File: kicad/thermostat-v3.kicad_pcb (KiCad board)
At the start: 2 copper layers, 140 x 64 mm, 91 parts, among them J1 HVAC R C W Y G, J2 USB-C, J3 Stemma QT, J4 2.9in EPD FPC, Q1 SI1308EDL, Q2 BT136S-600D, Q3 BT136S-600D, Q4 BT136S-600D, SW1 RESET, SW2 BOOT, SW3 UP, SW4 DOWN, SW5 MODE, U1 LMR16006XDDCR, U2 USBLC6-2SC6, U3 ESP32-C6-WROOM-1-N8, U4 STWD100NYWY3F, U5 SHT40-AD1B, U6 MOC3063S, U7 MOC3063S, U8 MOC3063S

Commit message: Display fit check: GDEY029T94 placement, fold geometry, overlay image; move panel outline on Cmts.User
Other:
- board text added: "2.9in EPD outline, 5mm above PCB (FPC exits right edge, folded under, contacts down) - see fab/display-fit.png"
- board text removed: "2.9in EPD panel outline (FPC exits right edge, folded under, contacts down)"
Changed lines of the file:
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@@
 	)
 	(gr_line
-		(start 209 125)
-		(end 209 161.7)
-		(stroke
-			(width 0.15)
-			(type default)
-		)
-		(layer "Cmts.User")
-	)
-	(gr_line
-		(start 209 161.7)
-		(end 130 161.7)
-		(stroke
-			(width 0.15)
-			(type default)
-		)
-		(layer "Cmts.User")
-	)
-	(gr_line
-		(start 130 125)
-		(end 209 125)
-		(stroke
-			(width 0.15)
-			(type default)
-		)
-		(layer "Cmts.User")
-	)
-	(gr_line
-		(start 130 161.7)
-		(end 130 125)
+		(start 208.46 126.24)
+		(end 208.46 162.94)
+		(stroke
+			(width 0.15)
+			(type default)
+		)
+		(layer "Cmts.User")
+	)
+	(gr_line
+		(start 208.46 162.94)
+		(end 129.46 162.94)
+		(stroke
+			(width 0.15)
+			(type default)
+		)
+		(layer "Cmts.User")
+	)
+	(gr_line
+		(start 129.46 126.24)
+		(end 208.46 126.24)
+		(stroke
+			(width 0.15)
+			(type default)
+		)
+		(layer "Cmts.User")
+	)
+	(gr_line
+		(start 129.46 162.94)
+		(end 129.46 126.24)
 		(stroke
 			(width 0.15)
@@
 		)
 	)
-	(gr_text "2.9in EPD panel outline (FPC exits right edge, folded under, contacts down)"
-		(at 169.5 126.5 0)
-		(layer "Cmts.User")
-		(effects
+	(gr_text "2.9in EPD outline, 5mm above PCB (FPC exits right edge, folded under, contacts down) - see fab/display-fit.png"
+		(at 169 127.7 0)
+		(layer "Cmts.User")
+		(effects

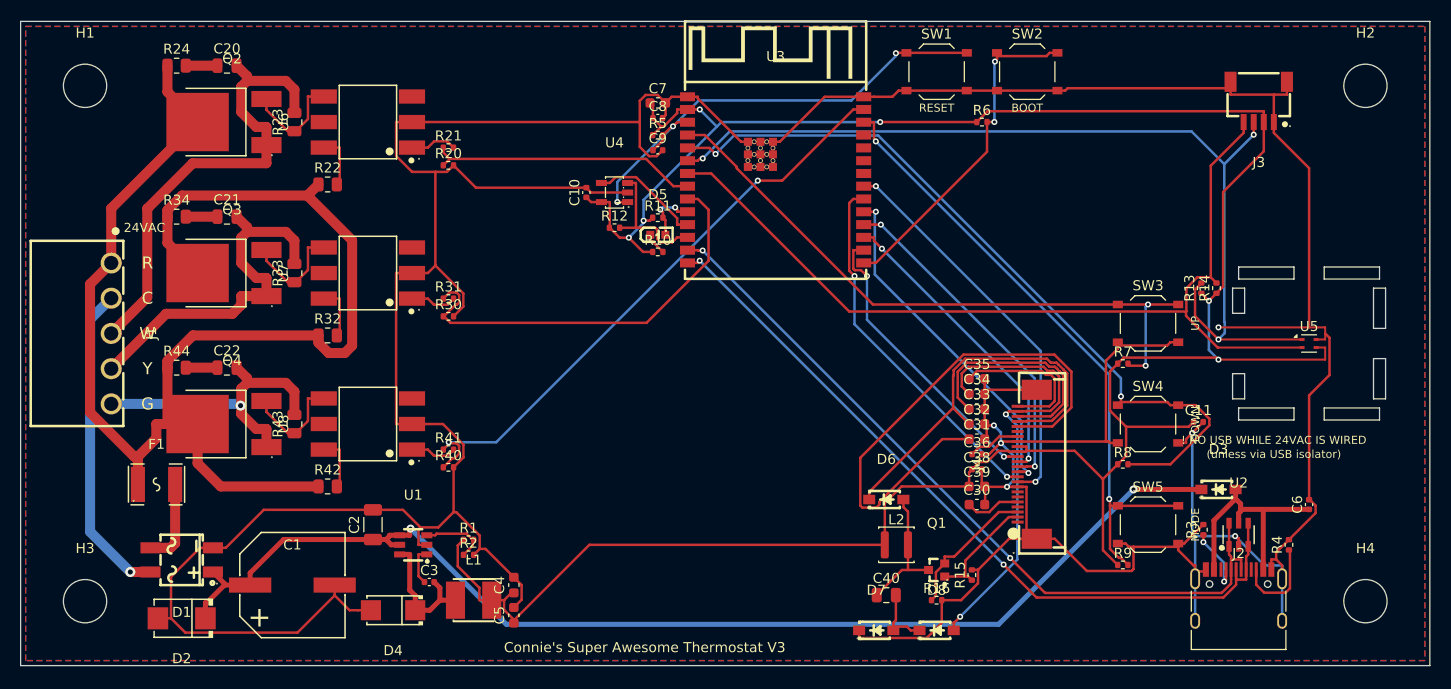
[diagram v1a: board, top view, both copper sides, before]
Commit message: V3 rev4: fix CPL/gerber origin, switch BOM grouping, basic-part swaps, silkscreen cleanup, cat logo
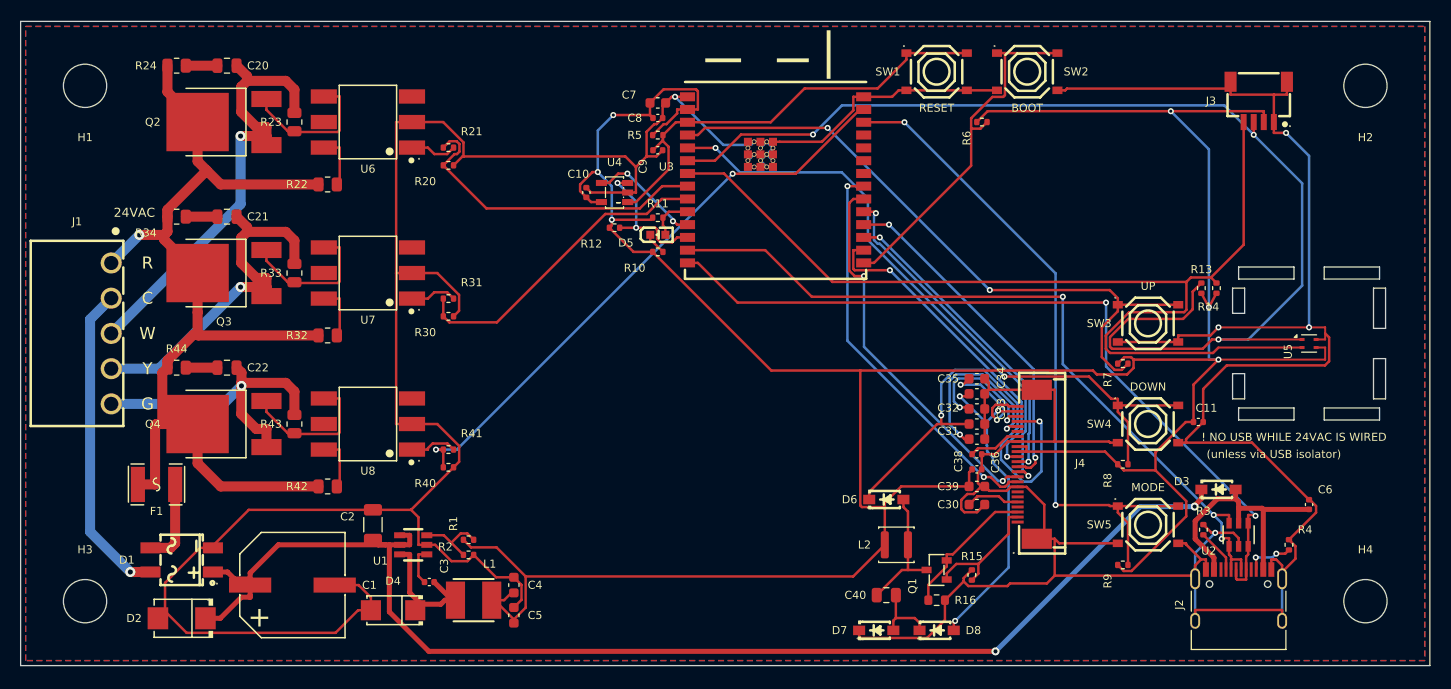
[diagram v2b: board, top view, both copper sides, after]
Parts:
- added LOGO1: LOGO, LOGO_CAT, B.Cu at (188.0, 145.0)
- C2: value 2.2uF 100V -> 2.2uF 50V
- Q1: value SI1308EDL -> AO3400A; footprint tstat:SOT-323_SI1308 -> tstat:SOT-23_AO3400A
- R16: footprint Resistor_SMD:R_0402_1005Metric -> Resistor_SMD:R_0603_1608Metric
- SW1, SW2, SW3, SW4, SW5: footprint Button_Switch_SMD:SW_Push_1P1T_XKB_TS-1187A -> tstat:SW_TS1187A
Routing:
- net +3V3: track 257.8 -> 314.0 mm
- net HVAC_R: track 141.8 -> 100.9 mm, vias 0 -> 1
- net EPD_VSH1: track 54.2 -> 18.6 mm, vias 0 -> 2
- net I2C_SDA: track 94.1 -> 121.4 mm
- net I2C_SCL: track 91.2 -> 107.3 mm
- net EPD_VGL: track 45.6 -> 32.2 mm, vias 2 -> 3
- net VIN_HV: track 117.5 -> 128.4 mm
- net EPD_VSL: track 23.4 -> 13.2 mm, vias 0 -> 2
- net DRV_Y: track 41.5 -> 31.3 mm
- net BTN_DOWN: track 76.7 -> 68.4 mm
- net EPD_VGH: track 39.7 -> 45.8 mm, vias 0 -> 2
- net DRV_W: track 27.0 -> 31.9 mm
- net BTN_MODE: track 62.4 -> 66.8 mm
- net CC2: track 9.22 -> 4.83 mm, vias 0 -> 2
- net GATE_Y: track 10.4 -> 14.3 mm
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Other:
- board text added: "Connie's Super Awesome Thermostat VERSION 3.0"
- board text removed: "Connie's Super Awesome Thermostat V3"

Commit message: V3 rev5: rear vertical HVAC terminal, low-profile C1, SHT40 island net rule, 3D-printable case (OpenSCAD/STL/3MF)
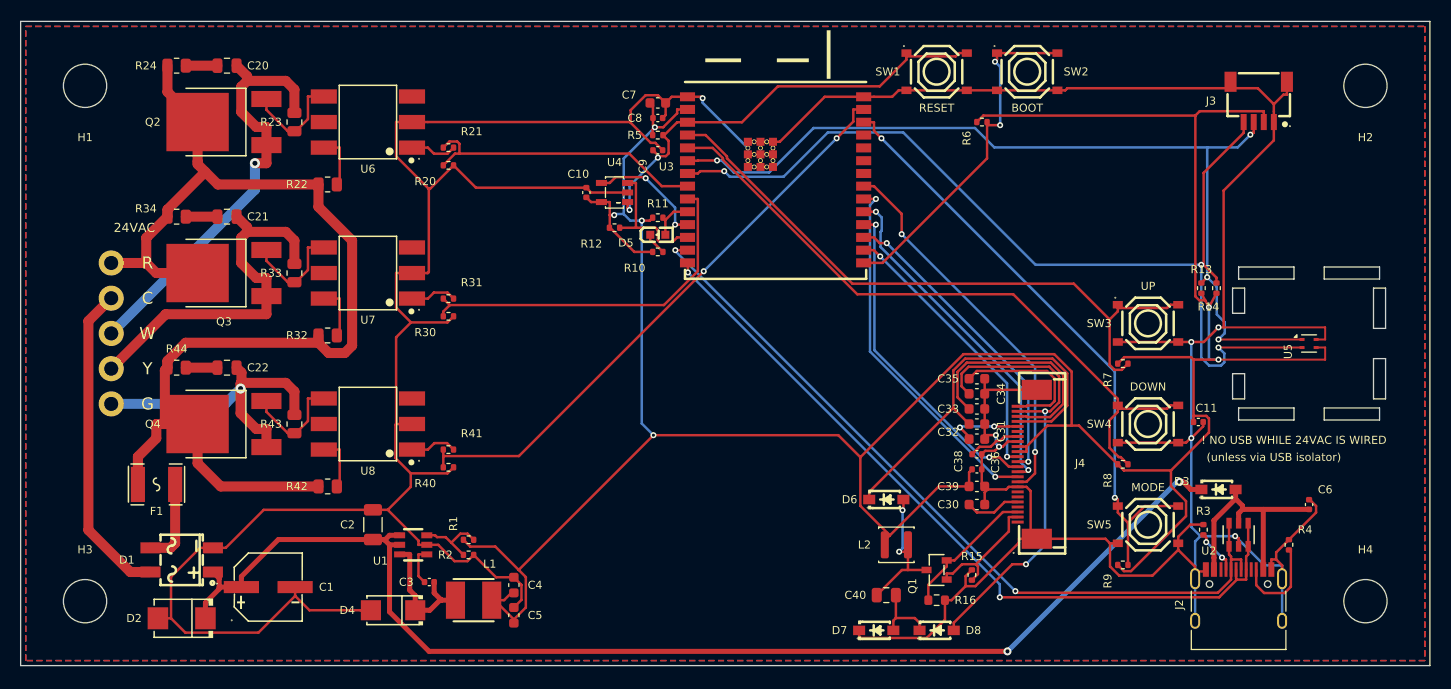
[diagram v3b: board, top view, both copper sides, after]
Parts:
- C1: value 100uF 63V -> 22uF 50V; footprint tstat:CP_10x10_RVT -> tstat:CP_6.3x5.4_RVT
- J1: footprint tstat:HVAC_TERM_15EDGRC -> tstat:HVAC_TERM_15EDGVC; moved to B.Cu
- moved C1 2.41 mm to (124.6, 156.2)
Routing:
- net I2C_SDA: track 121.4 -> 90.2 mm, vias 3 -> 4
- net GND: track 495.3 -> 464.3 mm, vias 5 -> 7
- net +3V3: track 314.0 -> 295.8 mm
- net HVAC_R: track 100.9 -> 116.4 mm, vias 1 -> 0
- net EPD_VGL: track 32.2 -> 46.1 mm, vias 3 -> 2
- net EPD_VSH1: track 18.6 -> 7.32 mm
- net EPD_VSL: track 13.2 -> 23.5 mm, vias 2 -> 0
- net I2C_SCL: track 107.3 -> 99.0 mm, vias 0 -> 3
- net EPD_VGH: track 45.8 -> 39.7 mm, vias 2 -> 0
- net BTN_MODE: track 66.8 -> 61.2 mm
- net DRV_Y: track 31.3 -> 36.5 mm
- net CC2: track 4.83 -> 9.31 mm, vias 2 -> 0
- net VIN_HV: track 128.4 -> 124.0 mm
- net EPD_MOSI: track 32.2 -> 28.1 mm
- net GATE_Y: track 14.3 -> 10.4 mm
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
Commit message: V3 rev6: drywall-anchor case (146x70), multi-colour AMS parts + 3MF, no USB opening, 100V X7R bulk caps
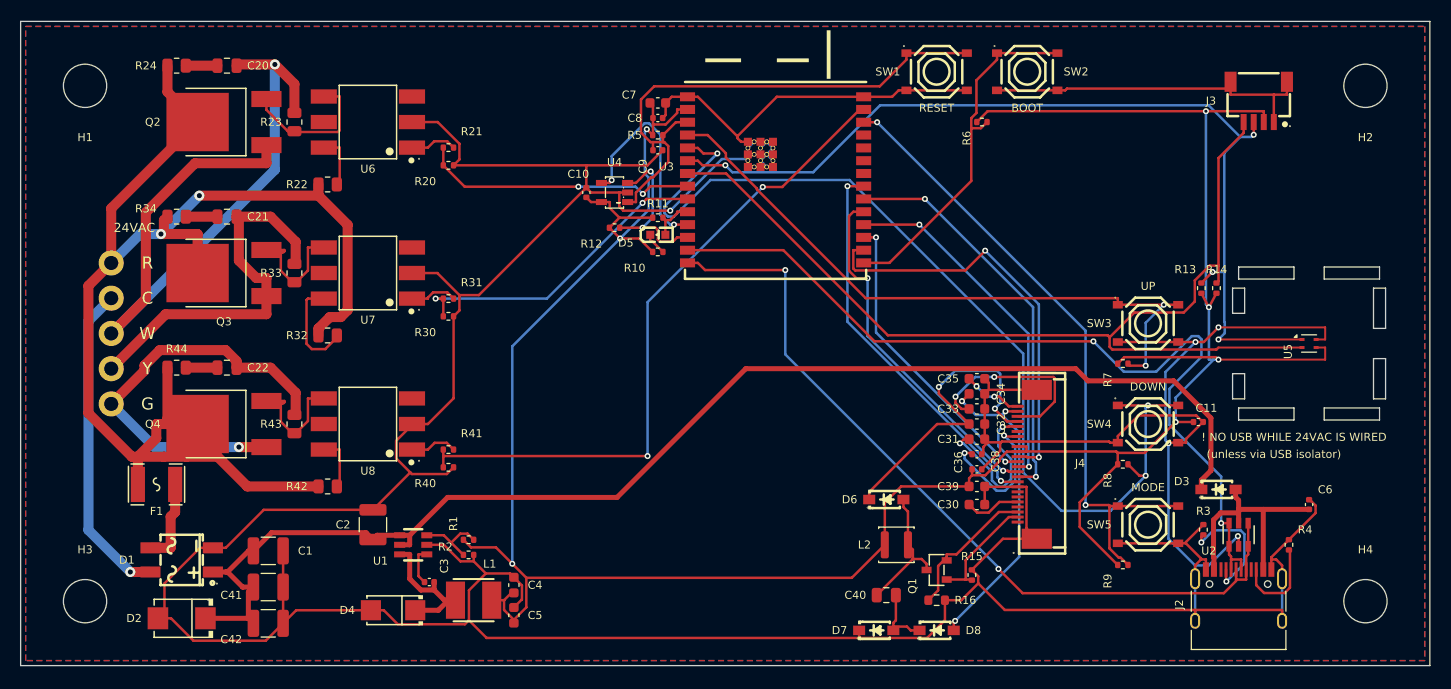
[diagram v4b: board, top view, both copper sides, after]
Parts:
- added C41: 4.7uF 100V X7R, Capacitor_SMD:C_1210_3225Metric, F.Cu at (124.6, 156.2)
- added C42: 4.7uF 100V X7R, Capacitor_SMD:C_1210_3225Metric, F.Cu at (124.6, 159.8)
- C1: value 22uF 50V -> 4.7uF 100V X7R; footprint tstat:CP_6.3x5.4_RVT -> Capacitor_SMD:C_1210_3225Metric
- C2: value 2.2uF 50V -> 4.7uF 100V X7R; footprint Capacitor_SMD:C_1206_3216Metric -> Capacitor_SMD:C_1210_3225Metric
- moved C1 3.60 mm to (124.6, 152.6)
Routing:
- net GND: track 464.3 -> 525.0 mm, vias 7 -> 5
- net BTN_DOWN: track 67.0 -> 98.0 mm, vias 0 -> 3
- net HVAC_W: track 43.3 -> 72.2 mm
- net +3V3: track 295.8 -> 271.4 mm, vias 6 -> 7
- net HVAC_R: track 116.4 -> 133.6 mm, vias 0 -> 2
- net EPD_VGL: track 46.1 -> 32.1 mm, vias 2 -> 3
- net EPD_MOSI: track 28.1 -> 41.7 mm
- net HVAC_G: track 31.2 -> 42.4 mm
- net WD_WDI: track 11.7 -> 21.3 mm
- net EPD_VCOM: track 15.3 -> 5.97 mm, vias 0 -> 2
- net EPD_VDD: track 5.26 -> 14.5 mm, vias 0 -> 2
- net EPD_VSH1: track 7.32 -> 16.2 mm
- net DRV_G: track 58.5 -> 66.7 mm
- net ESP_EN: track 45.4 -> 53.5 mm, vias 2 -> 0
- net USB_DN: track 78.8 -> 86.8 mm
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
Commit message: V3 rev7: rear right-angle HVAC terminal beside centred wire hole, deeper case standoffs
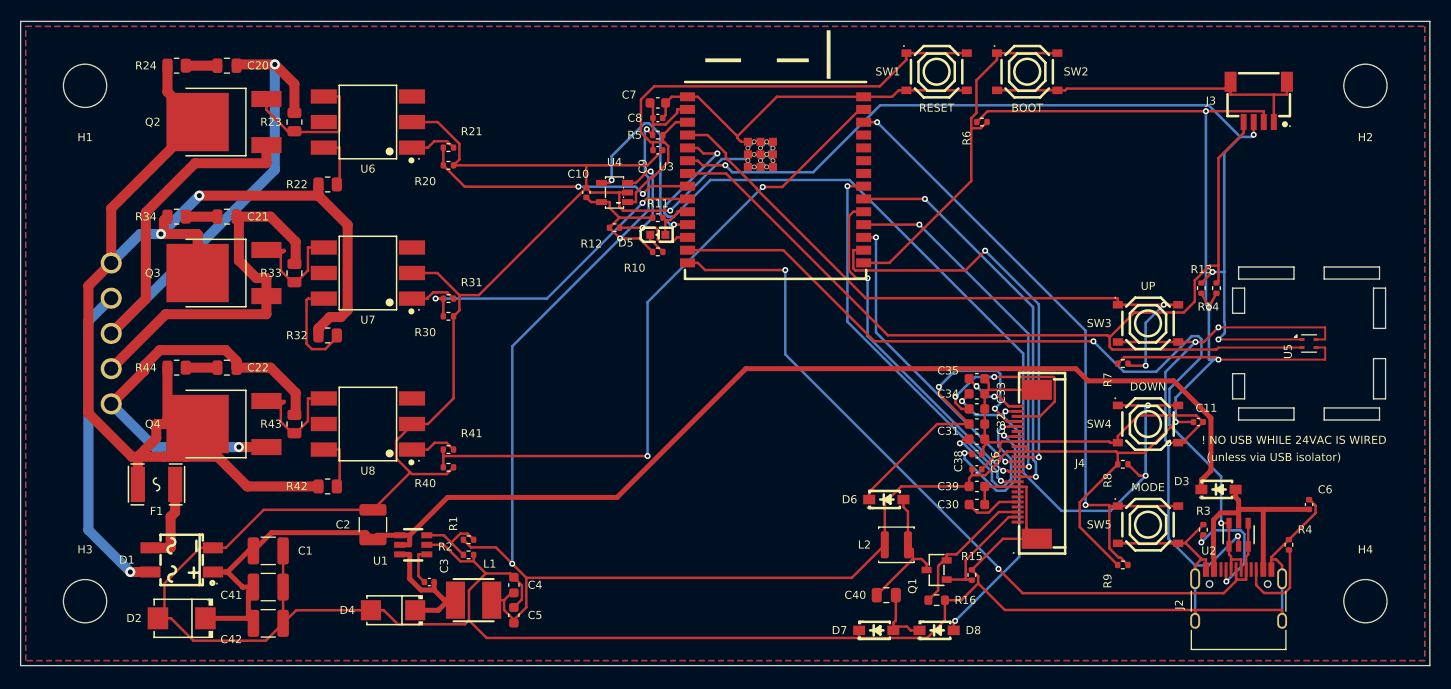
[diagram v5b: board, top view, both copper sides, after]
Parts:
- J1: footprint tstat:HVAC_TERM_15EDGVC -> tstat:HVAC_TERM_15EDGRC
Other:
- board text added: "24VAC HVAC (plug: 15EDGK-3.5-05P)"
- board text removed: "24VAC"

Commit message: Rev 8: review fixes - J1 really at (70,58) rear, D3 SS210 100V, F1 60V PTC, SHDN 100k, C43 47uF/63V rear THT, T435-600B standard-gate triacs, antenna keepout, USB-C flush, 1mm HV pour clearance, test pads; case RESET pinhole; generator scripts + review response
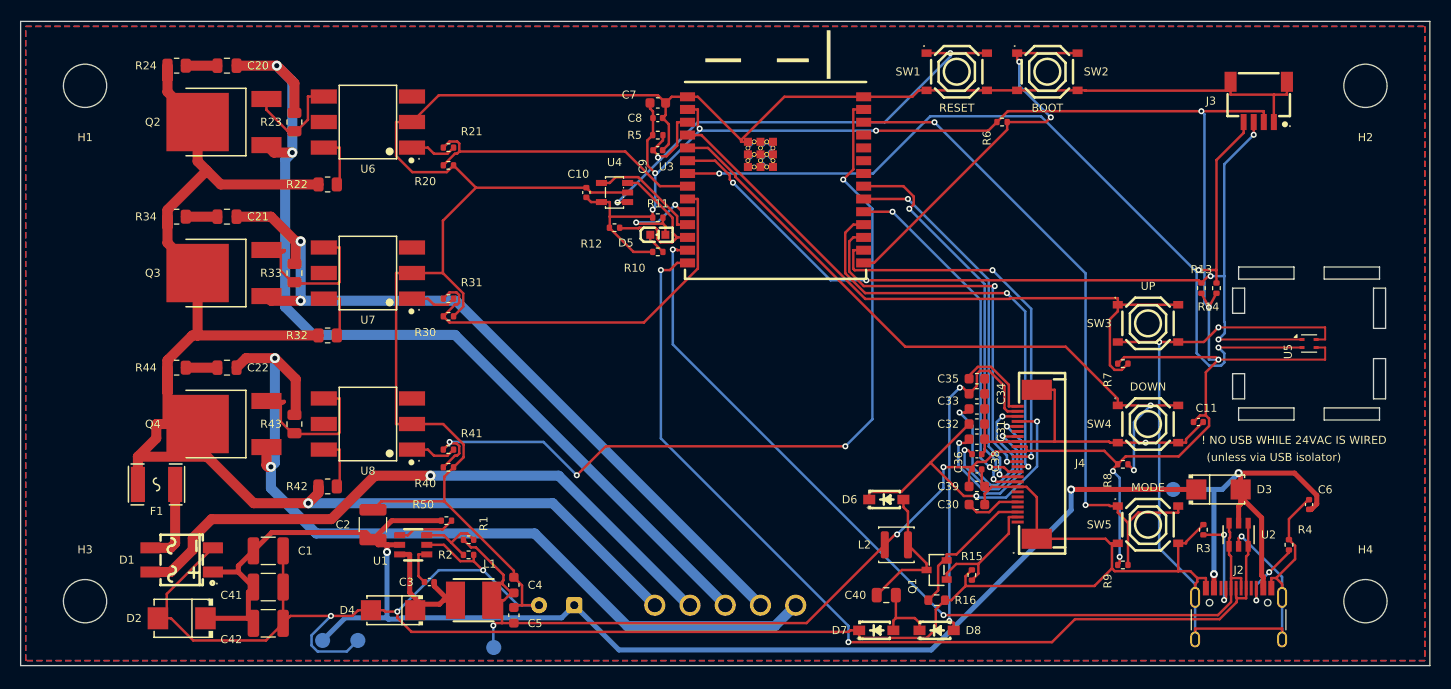
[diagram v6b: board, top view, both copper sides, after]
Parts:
- added C43: 47uF 63V, Capacitor_THT:CP_Radial_D8.0mm_P3.50mm, B.Cu at (155.0, 158.0)
- added R50: 100k, Resistor_SMD:R_0402_1005Metric, F.Cu at (142.3, 149.6)
- added TP1: VIN_HV, TestPoint:TestPoint_Pad_D1.5mm, B.Cu at (130.0, 161.5)
- added TP2: GND, TestPoint:TestPoint_Pad_D1.5mm, B.Cu at (133.5, 161.5)
- added TP3: +3V3, TestPoint:TestPoint_Pad_D1.5mm, B.Cu at (147.0, 162.2)
- added TP4: VBUS, TestPoint:TestPoint_Pad_D1.5mm, B.Cu at (214.5, 146.5)
- D3: value B5819W -> SS210; footprint tstat:SOD-123_B5819W -> tstat:SMA_SS210
- F1: value 0.5A PTC -> 0.5A 60V PTC
- Q2, Q3, Q4: value BT136S-600D -> T435-600B
- moved J1 66.7 mm to (170.0, 158.0), turned to 0 degrees
- moved LOGO1 45.5 mm to (145.0, 130.0)
- moved R6 2.00 mm to (197.5, 110.0)
- moved SW1 2.00 mm to (193.0, 105.0)
- moved SW2 2.00 mm to (202.0, 105.0)
- moved J2 1.85 mm to (221.0, 160.3)
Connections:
- U1 pad 4: VIN_HV -> BUCK_EN
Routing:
- net HVAC_G: track 42.4 -> 84.9 mm, vias 1 -> 2
- net HVAC_Y: track 38.3 -> 77.5 mm, vias 0 -> 2
- net HVAC_C: track 31.9 -> 63.6 mm
- net BTN_DOWN: track 98.0 -> 67.8 mm, vias 3 -> 2
- net GND: track 525.0 -> 548.8 mm, vias 5 -> 7
- net HVAC_W: track 72.2 -> 93.2 mm, vias 1 -> 2
- net VBUS: track 24.2 -> 42.7 mm, vias 0 -> 2
- net DRV_G: track 66.7 -> 84.1 mm, vias 2 -> 4
- net USB_DP: track 81.4 -> 97.7 mm
- net VIN_HV: track 131.0 -> 144.3 mm, vias 0 -> 2
- net WD_WDI: track 21.3 -> 11.2 mm, vias 2 -> 0
- net DRV_Y: track 31.7 -> 40.5 mm, vias 2 -> 0
- net EPD_SCK: track 30.1 -> 38.8 mm
- net HVAC_R: track 133.6 -> 140.7 mm, vias 2 -> 1
- net EPD_CS: track 35.2 -> 42.3 mm
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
